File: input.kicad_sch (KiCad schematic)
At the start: 0 parts

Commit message: Add debounce subsheet
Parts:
- added C64: 100nF, Capacitor_SMD:C_0402_1005Metric, symbol Device:C_Small
- added R32: 10k, Resistor_SMD:R_0402_1005Metric, symbol Device:R_Small
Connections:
- new net: C64.1, R32.1
- new net GND: C64.2

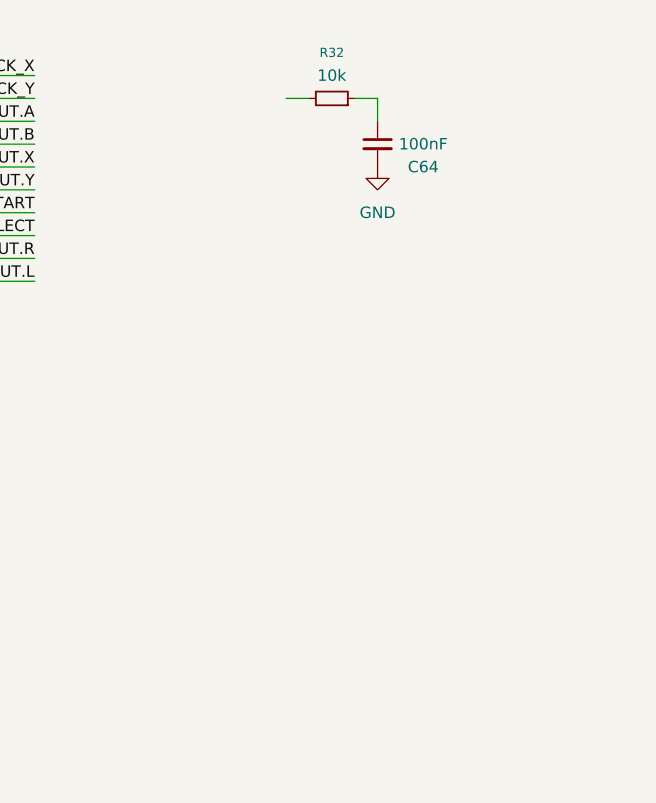
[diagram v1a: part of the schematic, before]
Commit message: Add ultra thin buttons for ABXY
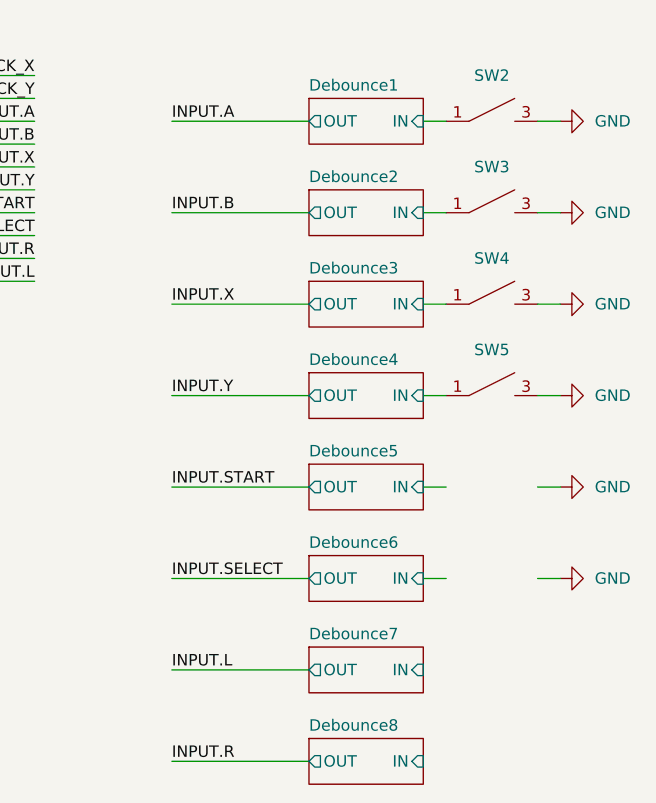
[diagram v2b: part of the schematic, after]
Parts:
- removed C64: 100nF, Capacitor_SMD:C_0402_1005Metric, symbol Device:C_Small
- removed R32: 10k, Resistor_SMD:R_0402_1005Metric, symbol Device:R_Small
- added SW2, SW3, SW4, SW5: TL3315NF100Q, custom:SW-SMD_4P-L4.5-W4.5-P3.50-LS4.8, symbol custom:TL3315NF100Q
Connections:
- net GND: now also SW2.3, SW2.4, SW3.3, SW3.4, SW4.3, SW4.4, SW5.3, SW5.4
- new net Debounce1/IN: SW2.1, SW2.2
- new net Debounce2/IN: SW3.1, SW3.2
- new net Debounce3/IN: SW4.1, SW4.2
- new net Debounce4/IN: SW5.1, SW5.2
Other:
- added sheet Debounce1 (debounce.kicad_sch)
- added sheet Debounce2 (debounce.kicad_sch)
- added sheet Debounce3 (debounce.kicad_sch)
- added sheet Debounce4 (debounce.kicad_sch)
- added sheet Debounce5 (debounce.kicad_sch)
- added sheet Debounce6 (debounce.kicad_sch)
- added sheet Debounce7 (debounce.kicad_sch)
- added sheet Debounce8 (debounce.kicad_sch)

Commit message: Add start and select buttons
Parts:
- added SW6: START, custom:SW-SMD_L3.9-W3.0-P4.45, symbol custom:TS-1088-AR02016
- added SW7: SELECT, custom:SW-SMD_L3.9-W3.0-P4.45, symbol custom:TS-1088-AR02016
- SW2: value TL3315NF100Q -> A
- SW3: value TL3315NF100Q -> B
- SW4: value TL3315NF100Q -> X
- SW5: value TL3315NF100Q -> Y
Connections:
- net Debounce5/IN: now also SW6.1
- net Debounce6/IN: now also SW7.1
- net GND: now also SW6.2, SW7.2

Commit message: Add L/R buttons
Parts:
- added SW8: L, custom:SW-SMD_L4.7-W3.5-P3.35-EH, symbol custom:TS-24CA-S26
- added SW9: R, custom:SW-SMD_L4.7-W3.5-P3.35-EH, symbol custom:TS-24CA-S26
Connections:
- net Debounce7/IN: now also SW8.1
- net Debounce8/IN: now also SW9.1
- net GND: now also SW8.2, SW9.2
- no-connect marks 0 -> 4

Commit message: Add joystick connector
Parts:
- added J10: 59453-042110ECHLF, custom:AMPHENOL_59453-042110ECHLF, symbol Connector_Generic_MountingPin:Conn_01x04_MountingPin
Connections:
- no-connect marks 4 -> 5
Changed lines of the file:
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@@
+	)
+	(no_connect
+		(at 175.26 101.6)
 	)
 	(no_connect
@@
 					(unit 1)
 				)
+			)
+		)
+	)
+	(symbol
+		(lib_id "Connector_Generic_MountingPin:Conn_01x04_MountingPin")
+		(at 175.26 91.44 0)
+		(unit 1)
+		(body_style 1)
+		(exclude_from_sim no)
+		(in_bom yes)
+		(on_board yes)
+		(in_pos_files yes)
+		(dnp no)
+		(fields_autoplaced yes)
+		(property "Reference" "J10"
+			(at 177.8 91.7955 0)
+			(show_name no)
+			(do_not_autoplace no)
+			(effects
+				(font
+					(size 1.27 1.27)
+				)
+				(justify left)
+			)
+		)
+		(property "Value" "59453-042110ECHLF"
+			(at 177.8 94.3355 0)
+			(show_name no)
+			(do_not_autoplace no)
+			(effects
+				(font
+					(size 1.27 1.27)
+				)
+				(justify left)
+			)
+		)
+		(property "Footprint" "custom:AMPHENOL_59453-042110ECHLF"
+			(at 175.26 91.44 0)
+			(hide yes)
+			(show_name no)
+			(do_not_autoplace no)
+			(effects
+				(font
+					(size 1.27 1.27)
+				)
+			)
+		)
+		(property "Datasheet" ""
+			(at 175.26 91.44 0)
+			(hide yes)
+			(show_name no)
+			(do_not_autoplace no)
+			(effects
+				(font
+					(size 1.27 1.27)
+				)
+			)
+		)
+		(property "Description" "Generic connectable mounting pin connector, single row, 01x04, script generated (kicad-library-utils/schlib/autogen/connector/)"
+			(at 175.26 91.44 0)
+			(hide yes)
+			(show_name no)
+			(do_not_autoplace no)
+			(effects
+				(font
+					(size 1.27 1.27)
+				)
+			)
+		)
+		(pin "3"
+		)
+		(pin "MP"
+		)
+		(pin "2"
+		)
+		(pin "4"
+		)
+		(pin "1"
+		)
+		(instances
+			(project "pedal"
+				(path "/e2443317-b83f-4e66-ac79-3186c6d613f3/08cc2b29-85b9-4aa1-81ca-cf2350ffd532"
+					(reference "J10")
+					(unit 1)
+				)

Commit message: Add joystick connections and lcsc part number
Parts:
- J10: LCSC (none) -> C3169529
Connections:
- net GND: now also J10.4 (Pin_4)
- net INPUT.STICK_X: now also J10.1 (Pin_1)
- net INPUT.STICK_Y: now also J10.3 (Pin_3)
- net +3V3: now reaches J10.2 (Pin_2)
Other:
- moved on the sheet: J10
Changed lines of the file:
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@@
 	)
 	(no_connect
-		(at 175.26 101.6)
+		(at 172.72 93.98)
 	)
 	(no_connect
@@
 	(wire
 		(pts
+			(xy 165.1 88.9) (xy 167.64 88.9)
+		)
+		(stroke
+			(width 0)
+			(type default)
+		)
+	)
+	(wire
+		(pts
+			(xy 165.1 81.28) (xy 167.64 81.28)
+		)
+		(stroke
+			(width 0)
+			(type default)
+		)
+	)
+	(wire
+		(pts
 			(xy 116.84 121.92) (xy 114.3 121.92)
 		)
@@
 	(wire
 		(pts
+			(xy 165.1 83.82) (xy 167.64 83.82)
+		)
+		(stroke
+			(width 0)
+			(type default)
+		)
+	)
+	(wire
+		(pts
 			(xy 101.6 101.6) (xy 104.14 101.6)
 		)
@@
 		(pts
 			(xy 116.84 91.44) (xy 114.3 91.44)
+		)
+		(stroke
+			(width 0)
+			(type default)
+		)
+	)
+	(wire
+		(pts
+			(xy 165.1 86.36) (xy 167.64 86.36)
 		)
 		(stroke
@@
 		)
 	)
+	(label "INPUT.STICK_X"
+		(at 165.1 81.28 180)
+		(effects
+			(font
+				(size 1.27 1.27)
+			)
+			(justify right)
+		)
+	)
 	(label "INPUT.STICK_Y"
 		(at 58.42 78.74 180)
@@
 			)
 			(justify right bottom)
+		)
+	)
+	(label "INPUT.STICK_Y"
+		(at 165.1 86.36 180)
+		(effects
+			(font
+				(size 1.27 1.27)
+			)
+			(justify right)
 		)
 	)
@@
 	(symbol
 		(lib_id "Connector_Generic_MountingPin:Conn_01x04_MountingPin")
-		(at 175.26 91.44 0)
+		(at 172.72 83.82 0)
 		(unit 1)
 		(body_style 1)
@@
 		(fields_autoplaced yes)
 		(property "Reference" "J10"
-			(at 177.8 91.7955 0)
+			(at 175.26 84.1755 0)
 			(show_name no)
 			(do_not_autoplace no)
@@
 		)
 		(property "Value" "59453-042110ECHLF"
-			(at 177.8 94.3355 0)
+			(at 175.26 86.7155 0)
 			(show_name no)
 			(do_not_autoplace no)
@@
 		)
 		(property "Footprint" "custom:AMPHENOL_59453-042110ECHLF"
-			(at 175.26 91.44 0)
+			(at 172.72 83.82 0)
 			(hide yes)
 			(show_name no)
@@
 		)
 		(property "Datasheet" ""
-			(at 175.26 91.44 0)
+			(at 172.72 83.82 0)
 			(hide yes)
 			(show_name no)
@@
 		)
 		(property "Description" "Generic connectable mounting pin connector, single row, 01x04, script generated (kicad-library-utils/schlib/autogen/connector/)"
-			(at 175.26 91.44 0)
+			(at 172.72 83.82 0)
+			(hide yes)
+			(show_name no)
+			(do_not_autoplace no)
+			(effects
+				(font
+					(size 1.27 1.27)
+				)
+			)
+		)
+		(property "LCSC" "C3169529"
+			(at 172.72 83.82 0)
 			(hide yes)
 			(show_name no)
@@
 	)
 	(symbol
+		(lib_id "power:+3V3")
+		(at 165.1 83.82 90)
+		(unit 1)
+		(body_style 1)
+		(exclude_from_sim no)
+		(in_bom yes)
+		(on_board yes)
+		(in_pos_files yes)
+		(dnp no)
+		(fields_autoplaced yes)
+		(property "Reference" "#PWR0138"
+			(at 168.91 83.82 0)
+			(hide yes)
+			(show_name no)
+			(do_not_autoplace no)
+			(effects
+				(font
+					(size 1.27 1.27)
+				)
+			)
+		)
+		(property "Value" "+3V3"
+			(at 161.29 83.8199 90)
+			(show_name no)
+			(do_not_autoplace no)
+			(effects
+				(font
+					(size 1.27 1.27)
+				)
+				(justify left)
+			)
+		)
+		(property "Footprint" ""
+			(at 165.1 83.82 0)
+			(hide yes)
+			(show_name no)
+			(do_not_autoplace no)
+			(effects
+				(font
+					(size 1.27 1.27)
+				)
+			)
+		)
+		(property "Datasheet" ""
+			(at 165.1 83.82 0)
+			(hide yes)
+			(show_name no)
+			(do_not_autoplace no)
+			(effects
+				(font
+					(size 1.27 1.27)
+				)
+			)
+		)
+		(property "Description" "Power symbol creates a global label with name \"+3V3\""
+			(at 165.1 83.82 0)
+			(hide yes)
+			(show_name no)
+			(do_not_autoplace no)
+			(effects
+				(font
+					(size 1.27 1.27)
+				)
+			)
+		)
+		(pin "1"
+		)
+		(instances
+			(project "pedal"
+				(path "/e2443317-b83f-4e66-ac79-3186c6d613f3/08cc2b29-85b9-4aa1-81ca-cf2350ffd532"
+					(reference "#PWR0138")
+					(unit 1)
+				)
+			)
+		)
+	)
+	(symbol
 		(lib_id "custom:TS-1088-AR02016")
 		(at 109.22 121.92 0)
@@
 					(unit 1)
 				)
+			)
+		)
+	)
+	(symbol
+		(lib_id "power:GND")
+		(at 165.1 88.9 270)
+		(unit 1)
+		(body_style 1)
+		(exclude_from_sim no)
+		(in_bom yes)
+		(on_board yes)
+		(in_pos_files yes)
+		(dnp no)
+		(fields_autoplaced yes)
+		(property "Reference" "#PWR0173"
+			(at 158.75 88.9 0)
+			(hide yes)
+			(show_name no)
+			(do_not_autoplace no)
+			(effects
+				(font
+					(size 1.27 1.27)
+				)
+			)
+		)
+		(property "Value" "GND"
+			(at 161.29 88.8999 90)
+			(show_name no)
+			(do_not_autoplace no)
+			(effects
+				(font
+					(size 1.27 1.27)
+				)
+				(justify right)
+			)
+		)
+		(property "Footprint" ""
+			(at 165.1 88.9 0)
+			(hide yes)
+			(show_name no)
+			(do_not_autoplace no)
+			(effects
+				(font
+					(size 1.27 1.27)
+				)
+			)
+		)
+		(property "Datasheet" ""
+			(at 165.1 88.9 0)
+			(hide yes)
+			(show_name no)
+			(do_not_autoplace no)
+			(effects
+				(font
+					(size 1.27 1.27)
+				)
+			)
+		)
+		(property "Description" "Power symbol creates a global label with name \"GND\" , ground"
+			(at 165.1 88.9 0)
+			(hide yes)
+			(show_name no)
+			(do_not_autoplace no)
+			(effects
+				(font
+					(size 1.27 1.27)
+				)
+			)
+		)
+		(pin "1"
+		)
+		(instances
+			(project "pedal"
+				(path "/e2443317-b83f-4e66-ac79-3186c6d613f3/08cc2b29-85b9-4aa1-81ca-cf2350ffd532"
+					(reference "#PWR0173")
+					(unit 1)
+				)
